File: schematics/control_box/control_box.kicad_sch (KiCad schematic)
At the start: 1 part

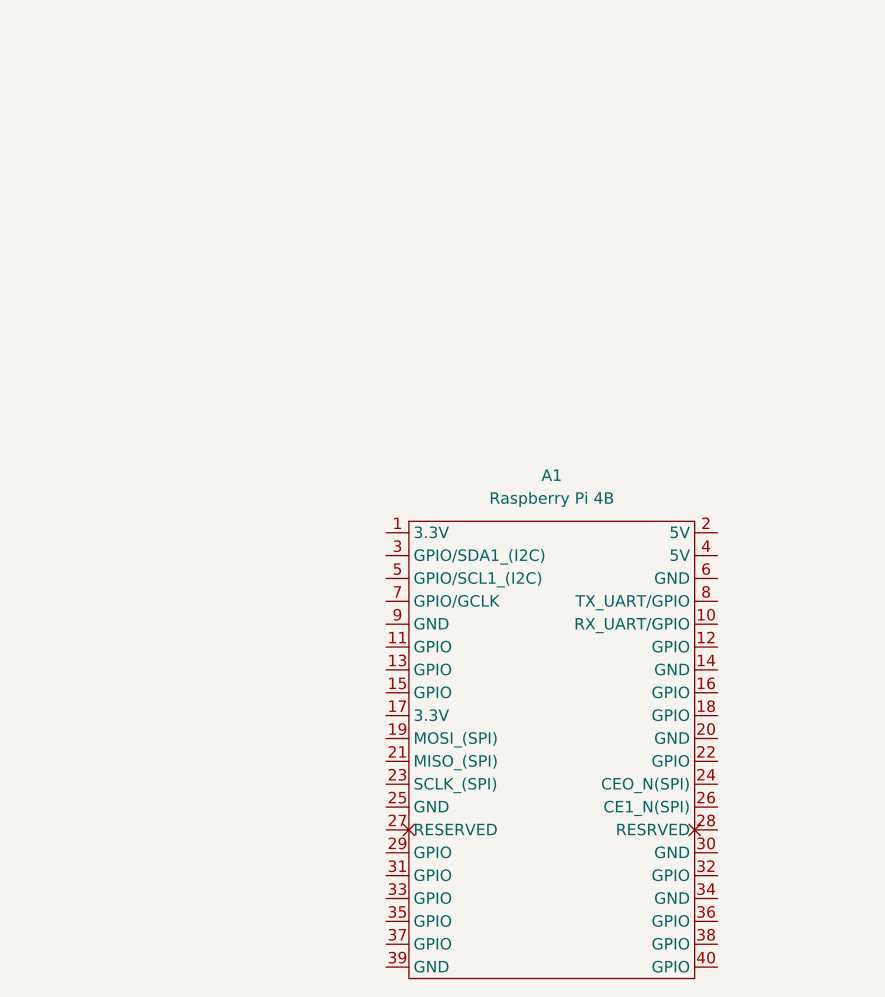
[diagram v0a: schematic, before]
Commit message: Added project schematic library
Project schematic library added.  120V to 5V (AC/DC) buck converter added and connected.
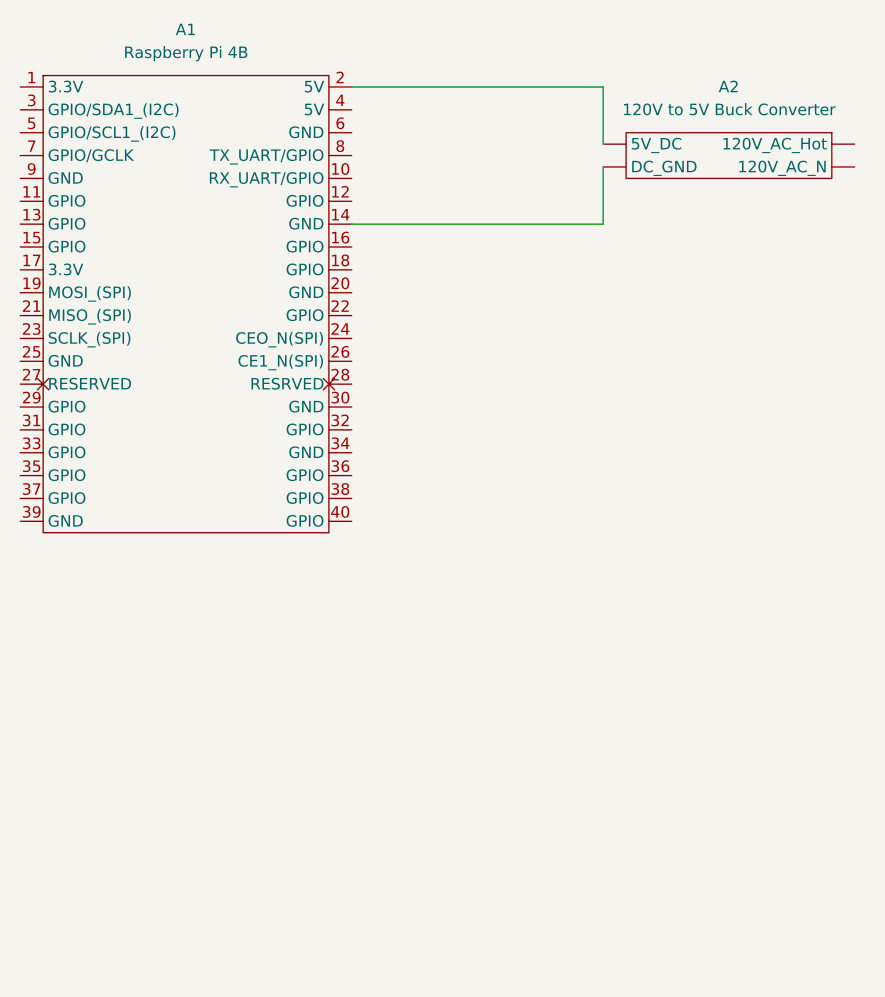
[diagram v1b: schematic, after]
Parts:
- removed A1: Raspberry Pi 4B, symbol rjwooda:Raspberry_Pi_4B
- added A1: Raspberry Pi 4B, symbol project_schematics:Raspberry_Pi_4B
- added A2: 120V to 5V Buck Converter, symbol project_schematics:120V_to_5V_Buck_Converter
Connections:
- new net: A1.14 (GND), A2. (DC_GND)
- new net: A1.2 (5V), A2. (DC_GND)
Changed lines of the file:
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@@
 	(generator_version "8.0")
 	(paper "A4")
+	(wire
+		(pts
+			(xy 92.71 30.48) (xy 92.71 24.13)
+		)
+		(stroke
+			(width 0)
+			(type default)
+		)
+	)
+	(wire
+		(pts
+			(xy 92.71 39.37) (xy 64.77 39.37)
+		)
+		(stroke
+			(width 0)
+			(type default)
+		)
+	)
+	(wire
+		(pts
+			(xy 92.71 24.13) (xy 64.77 24.13)
+		)
+		(stroke
+			(width 0)
+			(type default)
+		)
+	)
+	(wire
+		(pts
+			(xy 92.71 33.02) (xy 92.71 39.37)
+		)
+		(stroke
+			(width 0)
+			(type default)
+		)
+	)
 	(symbol
-		(lib_id "rjwooda:Raspberry_Pi_4B")
-		(at 86.36 96.52 0)
+		(lib_id "project_schematics:120V_to_5V_Buck_Converter")
+		(at 106.68 31.75 0)
+		(mirror y)
+		(unit 1)
+		(exclude_from_sim no)
+		(in_bom yes)
+		(on_board yes)
+		(dnp no)
+		(property "Reference" "A2"
+			(at 106.68 24.13 0)
+			(effects
+				(font
+					(size 1.27 1.27)
+				)
+			)
+		)
+		(property "Value" "120V to 5V Buck Converter"
+			(at 106.68 26.67 0)
+			(effects
+				(font
+					(size 1.27 1.27)
+				)
+			)
+		)
+		(property "Footprint" ""
+			(at 106.68 31.75 0)
+			(effects
+				(font
+					(size 1.27 1.27)
+				)
+				(hide yes)
+			)
+		)
+		(property "Datasheet" ""
+			(at 106.68 31.75 0)
+			(effects
+				(font
+					(size 1.27 1.27)
+				)
+				(hide yes)
+			)
+		)
+		(property "Description" ""
+			(at 106.68 31.75 0)
+			(effects
+				(font
+					(size 1.27 1.27)
+				)
+				(hide yes)
+			)
+		)
+		(pin ""
+		)
+		(pin ""
+		)
+		(pin ""
+		)
+		(pin ""
+		)
+		(instances
+			(project "control_box"
+				(path "/3ae0053d-206d-4787-aced-ee74b4da0e02"
+					(reference "A2")
+					(unit 1)
+				)
+			)
+		)
+	)
+	(symbol
+		(lib_id "project_schematics:Raspberry_Pi_4B")
+		(at 45.72 46.99 0)
 		(unit 1)
 		(exclude_from_sim no)
@@
 		(fields_autoplaced yes)
 		(property "Reference" "A1"
-			(at 86.995 67.31 0)
+			(at 46.355 17.78 0)
 			(effects
 				(font
@@
 		)
 		(property "Value" "Raspberry Pi 4B"
-			(at 86.995 69.85 0)
+			(at 46.355 20.32 0)
 			(effects
 				(font
@@
 		)
 		(property "Footprint" ""
-			(at 81.28 69.85 0)
+			(at 40.64 20.32 0)
 			(effects
 				(font
@@
 		)
 		(property "Datasheet" ""
-			(at 81.28 69.85 0)
+			(at 40.64 20.32 0)
 			(effects
 				(font
@@
 		)
 		(property "Description" ""
-			(at 81.28 69.85 0)
-			(effects
-				(font
-					(size 1.27 1.27)
-				)
-				(hide yes)
-			)
+			(at 40.64 20.32 0)
+			(effects
+				(font
+					(size 1.27 1.27)
+				)
+				(hide yes)
+			)
+		)
+		(pin "25"
+		)
+		(pin "28"
+		)
+		(pin "20"
+		)
+		(pin "11"
+		)
+		(pin "17"
+		)
+		(pin "2"
+		)
+		(pin "27"
+		)
+		(pin "29"
+		)
+		(pin "3"
+		)
+		(pin "21"
+		)
+		(pin "30"
+		)
+		(pin "26"
+		)
+		(pin "14"
+		)
+		(pin "18"
+		)
+		(pin "1"
+		)
+		(pin "10"
+		)
+		(pin "12"
 		)
 		(pin "13"
 		)
-		(pin "21"
+		(pin "15"
+		)
+		(pin "19"
+		)
+		(pin "22"
 		)
 		(pin "23"
 		)
-		(pin "18"
-		)
-		(pin "26"
-		)
-		(pin "28"
-		)
-		(pin "10"
-		)
-		(pin "29"
-		)
-		(pin "1"
-		)
-		(pin "12"
-		)
-		(pin "2"
-		)
-		(pin "11"
-		)
-		(pin "15"
-		)
-		(pin "17"
-		)
-		(pin "20"
-		)
-		(pin "22"
-		)
-		(pin "27"
+		(pin "16"
 		)
 		(pin "24"
 		)
-		(pin "14"
-		)
-		(pin "16"
-		)
-		(pin "19"
-		)
-		(pin "25"
+		(pin "38"
+		)
+		(pin "7"
+		)
+		(pin "6"
+		)
+		(pin "36"
+		)
+		(pin "34"
+		)
+		(pin "35"
+		)
+		(pin "8"
+		)
+		(pin "39"
+		)
+		(pin "37"
+		)
+		(pin "9"
+		)
+		(pin "5"
+		)
+		(pin "32"
+		)
+		(pin "40"
+		)
+		(pin "4"
+		)
+		(pin "31"
 		)
 		(pin "33"
 		)
-		(pin "7"
-		)
-		(pin "40"
-		)
-		(pin "8"
-		)
-		(pin "4"
-		)
-		(pin "30"
-		)
-		(pin "3"
-		)
-		(pin "36"
-		)
-		(pin "35"
-		)
-		(pin "34"
-		)
-		(pin "5"
-		)
-		(pin "6"
-		)
-		(pin "32"
-		)
-		(pin "31"
-		)
-		(pin "9"
-		)
-		(pin "38"
-		)
-		(pin "37"
-		)
-		(pin "39"
-		)
 		(instances

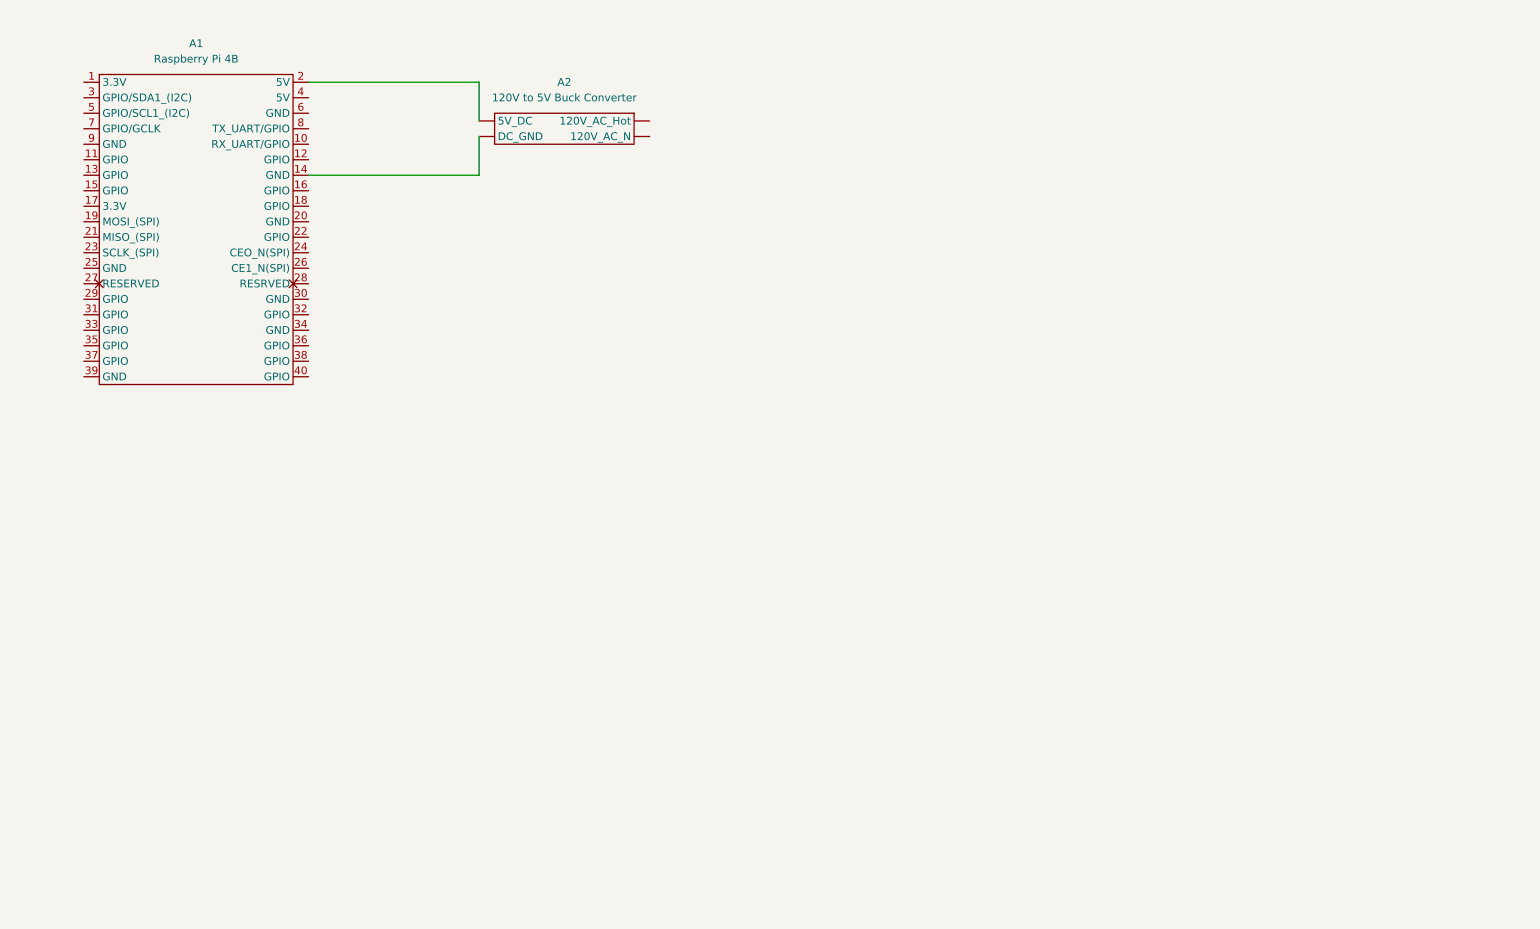
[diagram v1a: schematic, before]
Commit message: Complete electrical schematic
Completes a basic schematic with enough information to re-create the project wiring.
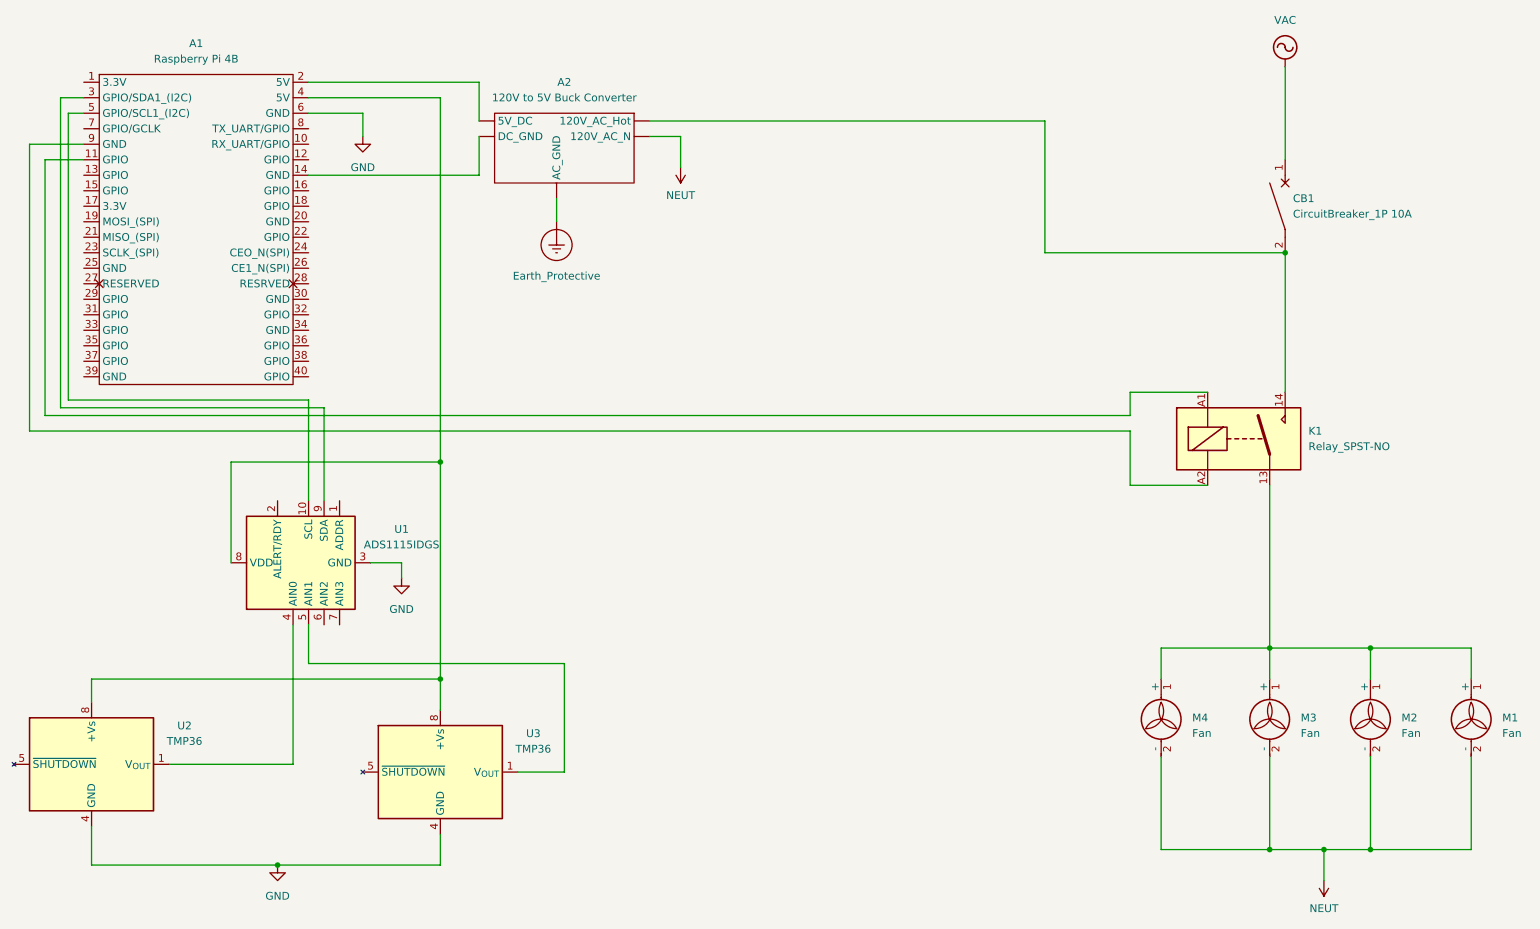
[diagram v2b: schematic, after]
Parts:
- added CB1: CircuitBreaker_1P 10A, symbol Device:CircuitBreaker_1P
- added K1: Relay_SPST-NO, symbol Relay:Relay_SPST-NO
- added M1, M2, M3, M4: Fan, symbol Motor:Fan
- added U1: ADS1115IDGS, Package_SO:TSSOP-10_3x3mm_P0.5mm, symbol Analog_ADC:ADS1115IDGS
- added U2, U3: TMP36, Package_SO:SOIC-8_3.9x4.9mm_P1.27mm, symbol project_schematics:TMP36
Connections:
- net NEUT: now reaches A2. (DC_GND)
- net NEUT: now also M1.2 (-), M2.2 (-), M3.2 (-), M4.2 (-)
- net at A1.11 (GPIO): now also K1.A1
- net at A1.3 (GPIO/SDA1_(I2C)): now also U1.9 (SDA)
- net at A1.4 (5V): now also U1.8 (VDD), U2.8 (+Vs), U3.8 (+Vs)
- net at A1.5 (GPIO/SCL1_(I2C)): now also U1.10 (SCL)
- net GND: now reaches A1.6 (GND)
- net GND: now also U1.3 (GND), U2.4 (GND), U3.4 (GND)
- net at A1.9 (GND): now also K1.A2
- new net: U1.5 (AIN1), U3.1 (V_{OUT})
- new net: A2. (DC_GND), CB1.2, K1.14
- new net: K1.13, M1.1 (+), M2.1 (+), M3.1 (+), M4.1 (+)
- new net: U1.4 (AIN0), U2.1 (V_{OUT})
- new net Earth_Protective: A2. (DC_GND)
- new net VAC: CB1.1
